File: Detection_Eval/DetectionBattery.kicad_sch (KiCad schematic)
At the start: 1 part

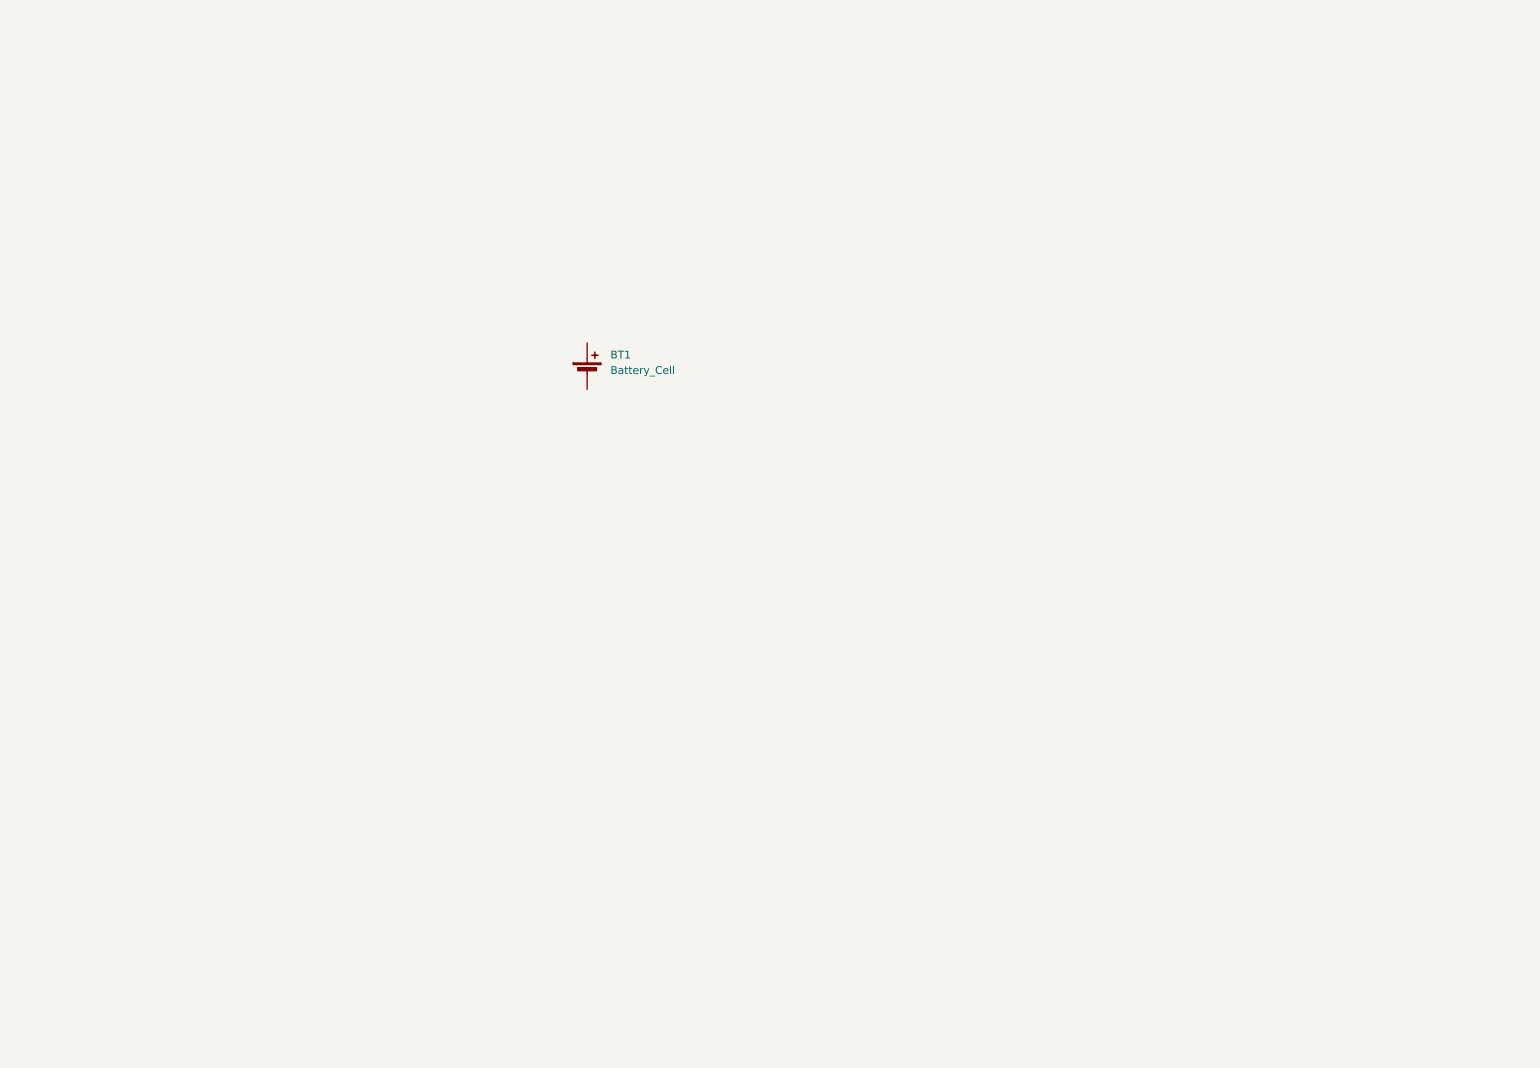
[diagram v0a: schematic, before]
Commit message: Madison_02-05
1.2V to 5V battery regulator added
chose AAAA 600maH rechargeable battery
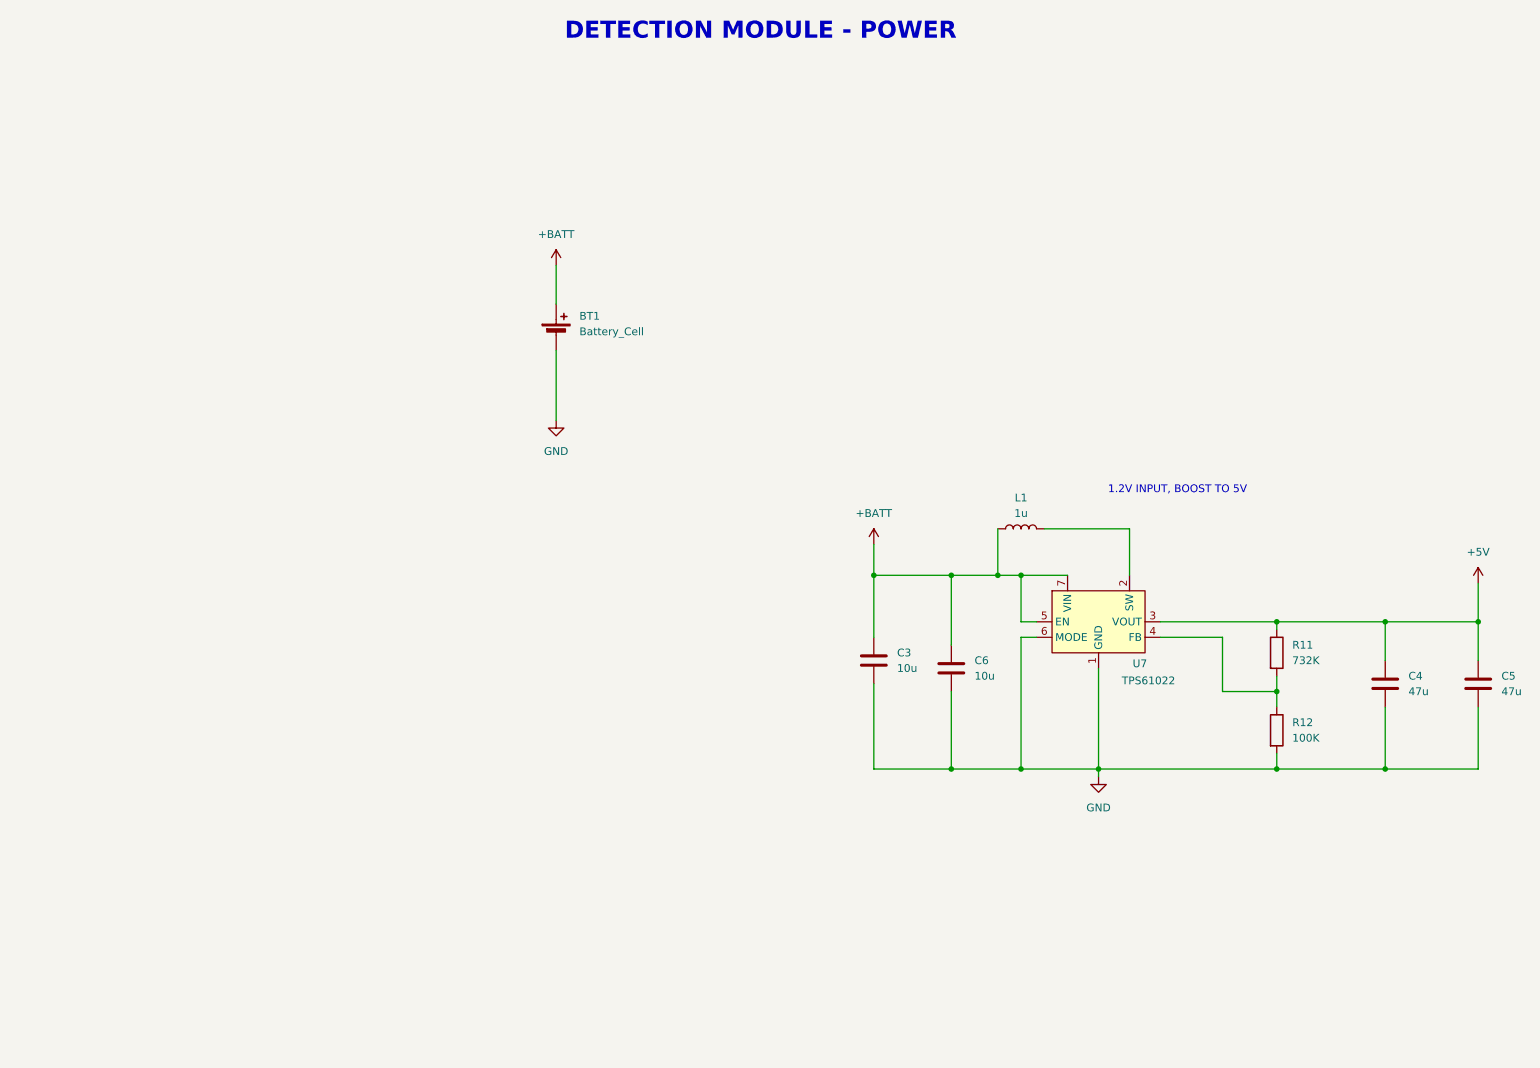
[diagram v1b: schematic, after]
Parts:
- added C3, C6: 10u, symbol Device:C
- added C4, C5: 47u, symbol Device:C
- added L1: 1u, symbol Device:L
- added R11: 732K, symbol Device:R
- added R12: 100K, symbol Device:R
- added U7: TPS61022, Package_DFN_QFN:Texas_RWU0007A_VQFN-7_2x2mm_P0.5mm, symbol Converter_DCDC:TPS61022
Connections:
- net +BATT: now reaches BT1.1 (+)
- net +BATT: now also C3.1, C6.1, L1.1, U7.5 (EN), U7.7 (VIN)
- net GND: now reaches BT1.2 (-)
- net GND: now also C3.2, C4.2, C5.2, C6.2, R12.2, U7.1 (GND), U7.6 (MODE)
- new net: R11.2, R12.1, U7.4 (FB)
- new net: L1.2, U7.2 (SW)
- new net +5V: C4.1, C5.1, R11.1, U7.3 (VOUT)
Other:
- note added: "1.2V INPUT, BOOST TO 5V"
- note added: "DETECTION MODULE - POWER"
- moved on the sheet: BT1

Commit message: Madison_02-05_2
Added battery charger circuit
Added footprints to accelerometer, lcd screen, buttons, AND gate, batt charger, batt holder
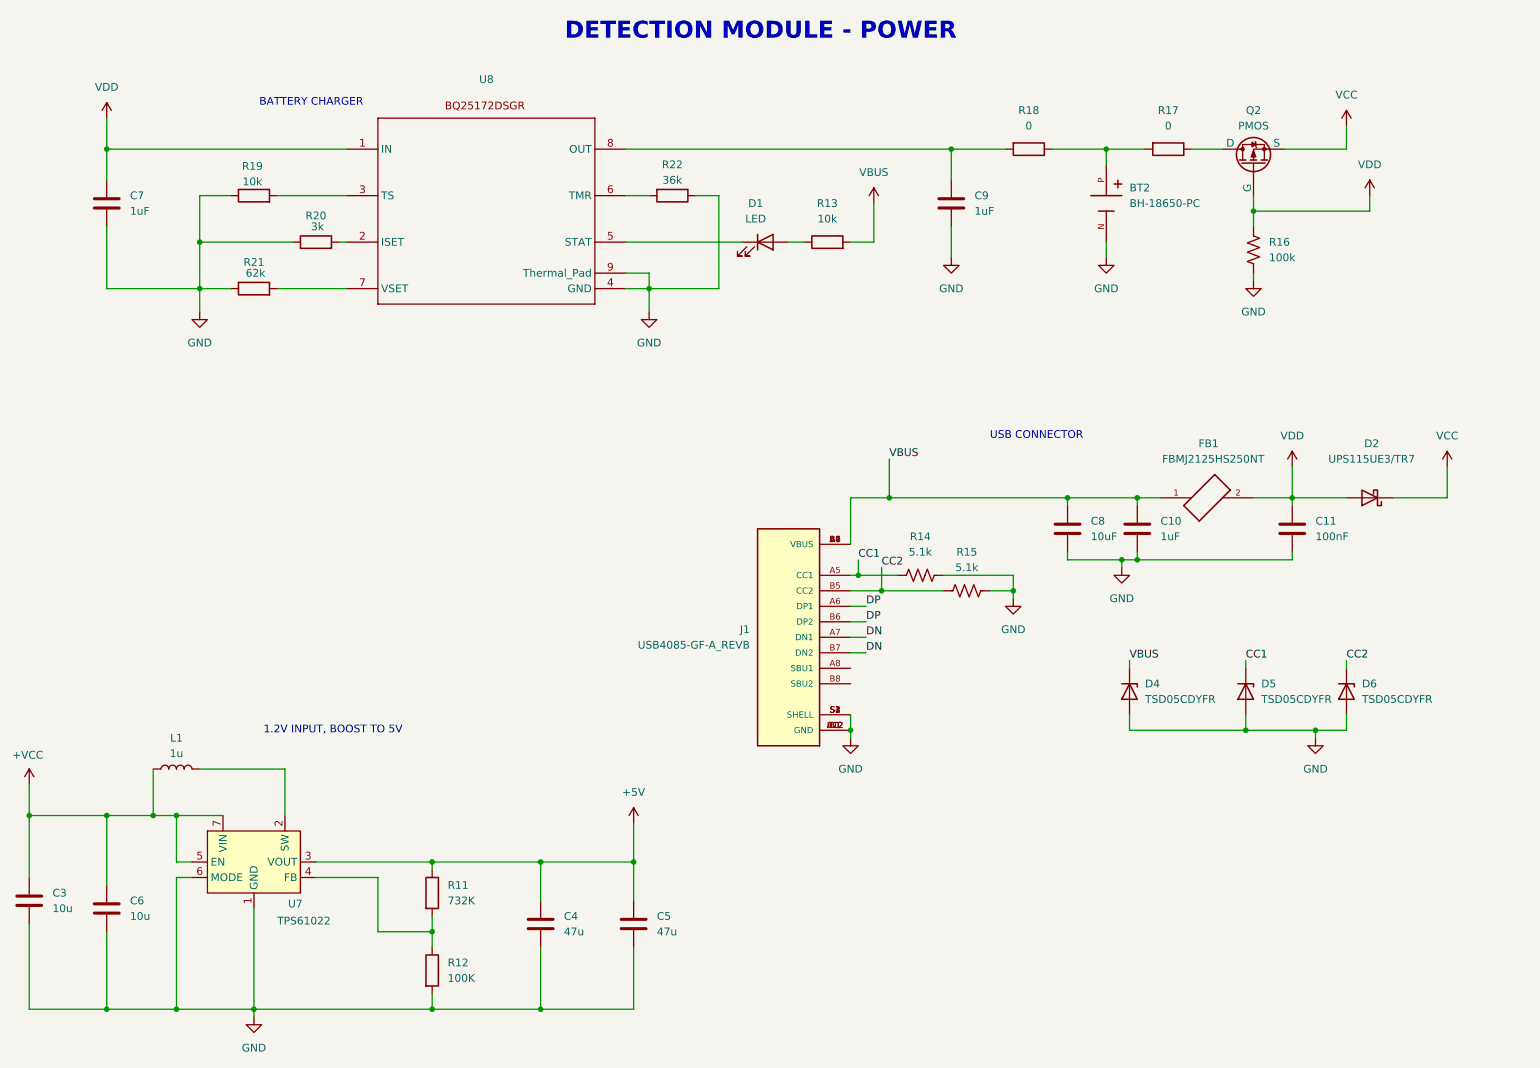
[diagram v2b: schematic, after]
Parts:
- removed BT1: Battery_Cell, symbol Device:Battery_Cell
- added BT2: BH-18650-PC, Detection_Eval_lib_fp:BAT_BEAAAAPC, symbol BH-18650-PC:BH-18650-PC
- added C10, C7, C9: 1uF, Capacitor_SMD:C_0603_1608Metric, symbol Device:C
- added C11: 100nF, Capacitor_SMD:C_0603_1608Metric, symbol Device:C
- added C8: 10uF, Capacitor_SMD:C_0603_1608Metric, symbol Device:C
- added D1: LED, LED_SMD:LED_0402_1005Metric_Pad0.77x0.64mm_HandSolder, symbol Device:LED
- added D2: UPS115UE3/TR7, Footprints:POWERMITE1_DO-216AA_MIS_MCH, symbol Device:D_Schottky
- added D4, D5, D6: TSD05CDYFR, Footprints:TVS_SOD2_DYF_TEX-L, symbol Diode:PTVS5V0Z1USK
- added FB1: FBMJ2125HS250NT, Footprints:BEADC2012X105N, symbol FBMJ2125HS250NT:FBMJ2125HS250NT
- added J1: USB4085-GF-A_REVB, Footprints:GCT_USB4085-GF-A_REVB, symbol USB4085-GF-A_REVB:USB4085-GF-A_REVB
- added Q2: PMOS, Footprints:SOT65P210X110-3N, symbol Simulation_SPICE:PMOS
- added R13, R19: 10k, Resistor_SMD:R_0402_1005Metric, symbol Device:R
- added R14, R15: 5.1k, Resistor_SMD:R_0603_1608Metric, symbol Device:R_US
- added R16: 100k, Resistor_SMD:R_0603_1608Metric, symbol Device:R_US
- added R17, R18: 0, Resistor_SMD:R_0402_1005Metric, symbol Device:R
- added R20: 3k, Resistor_SMD:R_0402_1005Metric, symbol Device:R
- added R21: 62k, Resistor_SMD:R_0402_1005Metric, symbol Device:R
- added R22: 36k, Resistor_SMD:R_0402_1005Metric, symbol Device:R
- added U8: ~, Detection_Eval_lib_fp:BQ25172DSGR, symbol Detection_Eval_lib:BQ25172DSGR
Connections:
- net GND: now also BT2.N, C10.2, C11.2, C7.2, C8.2, C9.2, D4.2 (A), D5.2 (A), D6.2 (A), J1.A1 (GND), J1.A12 (GND), J1.B1 (GND), J1.B12 (GND), J1.S1 (SHELL), J1.S2 (SHELL), J1.S3 (SHELL), J1.S4 (SHELL), R14.2, R15.2, R16.2, R19.1, R20.1, R21.1, R22.1, U8.4 (GND), U8.9 (Thermal_Pad)
- net +BATT renamed +VCC
- new net: R19.2, U8.3 (TS)
- new net: BT2.P, R17.2, R18.1
- new net: C9.1, R18.2, U8.8 (OUT)
- new net: R20.2, U8.2 (ISET)
- new net: D1.1 (K), U8.5 (STAT)
- new net: R22.2, U8.6 (TMR)
- new net: R21.2, U8.7 (VSET)
- new net: D1.2 (A), R13.1
- new net: Q2.1 (D), R17.1
- new net CC1: D5.1 (K), J1.A5 (CC1), R14.1
- new net CC2: D6.1 (K), J1.B5 (CC2), R15.1
- new net DN: J1.A7 (DN1), J1.B7 (DN2)
- new net DP: J1.A6 (DP1), J1.B6 (DP2)
- new net VBUS: C10.1, C8.1, D4.1 (K), FB1.1, J1.A4 (VBUS), J1.A9 (VBUS), J1.B4 (VBUS), J1.B9 (VBUS), R13.2
- new net VCC: D2.1 (K), Q2.3 (S)
- new net VDD: C11.1, C7.1, D2.2 (A), FB1.2, Q2.2 (G), R16.1, U8.1 (IN)
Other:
- note added: "BATTERY CHARGER"
- note added: "USB CONNECTOR"
- moved on the sheet: C3, C4, C5, C6, L1, R11, R12, U7

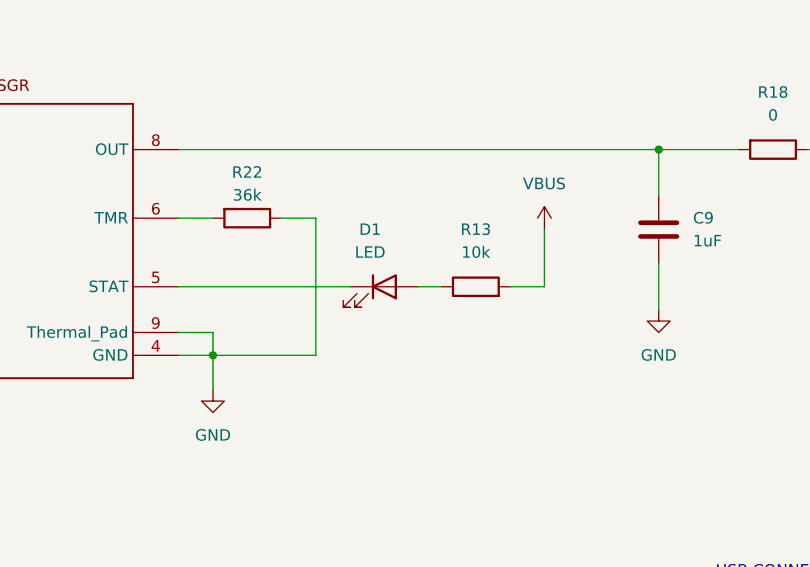
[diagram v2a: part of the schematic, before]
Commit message: Madison_02-06
final footprints added and layout positioning mostly done
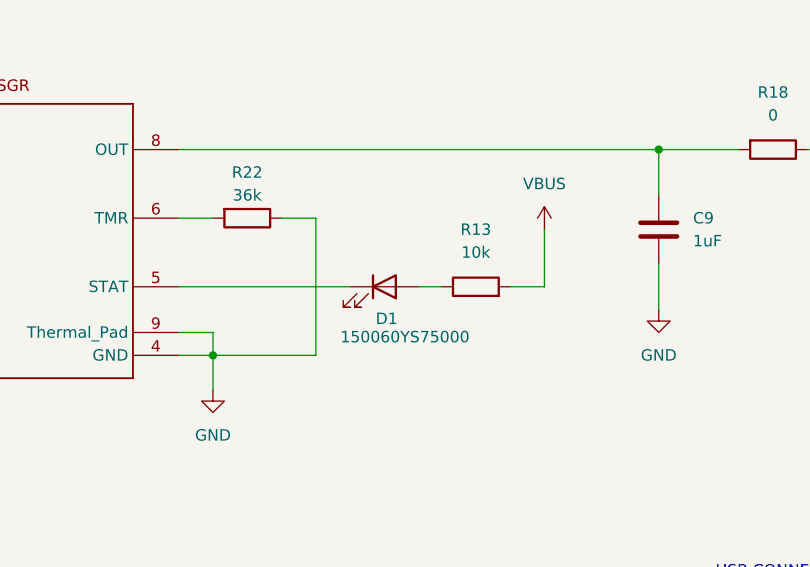
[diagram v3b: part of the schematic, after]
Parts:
- C3, C4, C5, C6: footprint (none) -> Capacitor_SMD:C_0603_1608Metric
- D1: value LED -> 150060YS75000; footprint LED_SMD:LED_0402_1005Metric_Pad0.77x0.64mm_HandSolder -> LED_SMD:LED_0201_0603Metric_Pad0.64x0.40mm_HandSolder
- L1: footprint (none) -> Detection_Eval_lib_fp:IND_IHLP-2020CZ
- R11: footprint (none) -> Resistor_SMD:R_0402_1005Metric
- R12: footprint (none) -> Resistor_SMD:R_0603_1608Metric
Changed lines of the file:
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@@
 			)
 		)
-		(property "Footprint" ""
+		(property "Footprint" "Resistor_SMD:R_0402_1005Metric"
 			(at 93.472 162.56 90)
 			(effects
@@
 			)
 		)
-		(property "Footprint" ""
+		(property "Footprint" "Capacitor_SMD:C_0603_1608Metric"
 			(at 42.8752 168.91 0)
 			(effects
@@
 			)
 		)
-		(property "Footprint" ""
+		(property "Footprint" "Resistor_SMD:R_0603_1608Metric"
 			(at 93.472 175.26 90)
 			(effects
@@
 			)
 		)
-		(property "Footprint" ""
+		(property "Footprint" "Detection_Eval_lib_fp:IND_IHLP-2020CZ"
 			(at 53.34 142.24 0)
 			(effects
@@
 			)
 		)
-		(property "Description" "Inductor"
+		(property "Description" "IHLP2020CZER1R0M01"
 			(at 53.34 142.24 0)
 			(effects
@@
 		(on_board yes)
 		(dnp no)
-		(fields_autoplaced yes)
 		(property "Reference" "D1"
-			(at 148.2725 49.53 0)
+			(at 150.114 59.436 0)
 			(effects
 				(font
@@
 			)
 		)
-		(property "Value" "LED"
-			(at 148.2725 52.07 0)
+		(property "Value" "150060YS75000"
+			(at 152.146 61.468 0)
 			(effects
 				(font
@@
 			)
 		)
-		(property "Footprint" "LED_SMD:LED_0402_1005Metric_Pad0.77x0.64mm_HandSolder"
+		(property "Footprint" "LED_SMD:LED_0201_0603Metric_Pad0.64x0.40mm_HandSolder"
 			(at 149.86 55.88 0)
 			(effects
@@
 			)
 		)
-		(property "Description" "Light emitting diode"
+		(property "Description" "150060YS75000 "
 			(at 149.86 55.88 0)
 			(effects
@@
 			)
 		)
-		(property "Footprint" ""
+		(property "Footprint" "Capacitor_SMD:C_0603_1608Metric"
 			(at 129.2352 171.45 0)
 			(effects
@@
 			)
 		)
-		(property "Footprint" ""
+		(property "Footprint" "Capacitor_SMD:C_0603_1608Metric"
 			(at 30.1752 167.64 0)
 			(effects
@@
 			)
 		)
-		(property "Footprint" ""
+		(property "Footprint" "Capacitor_SMD:C_0603_1608Metric"
 			(at 113.9952 171.45 0)
 			(effects

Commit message: LAYOUT DONE
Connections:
- net +VCC is gone; now on net VCC: C3.1, C6.1, L1.1, U7.5 (EN), U7.7 (VIN)
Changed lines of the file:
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@@
 			)
 		)
-		(property "Value" "+VCC"
+		(property "Value" "VCC"
 			(at 26.416 139.954 0)
 			(effects
